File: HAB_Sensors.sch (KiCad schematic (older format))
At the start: 20 parts, among them U10 LM4030, U7 MCP9808T, U8 BME280, U9 LSM9DS1

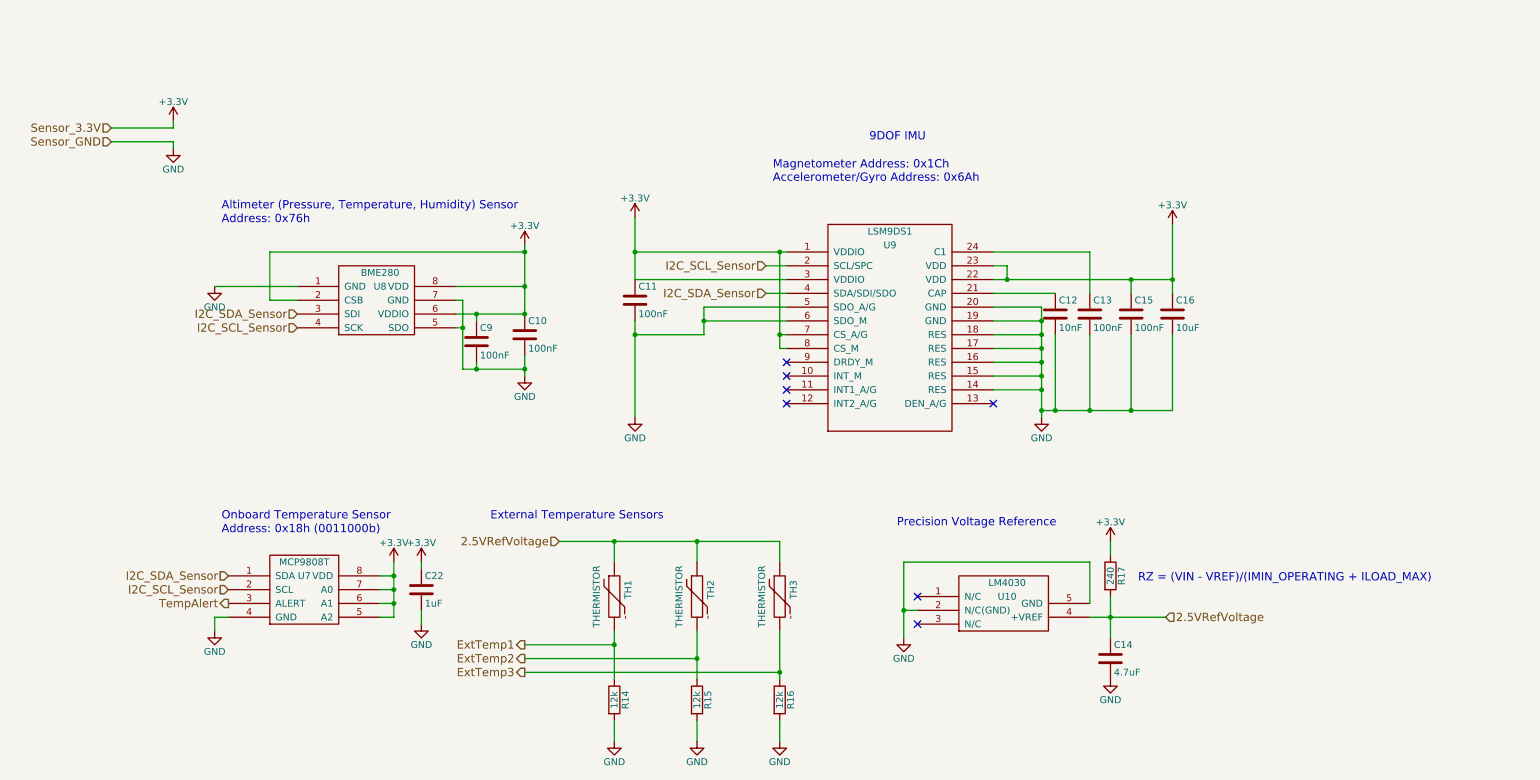
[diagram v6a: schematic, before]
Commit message: rev 2 of hab board in progress
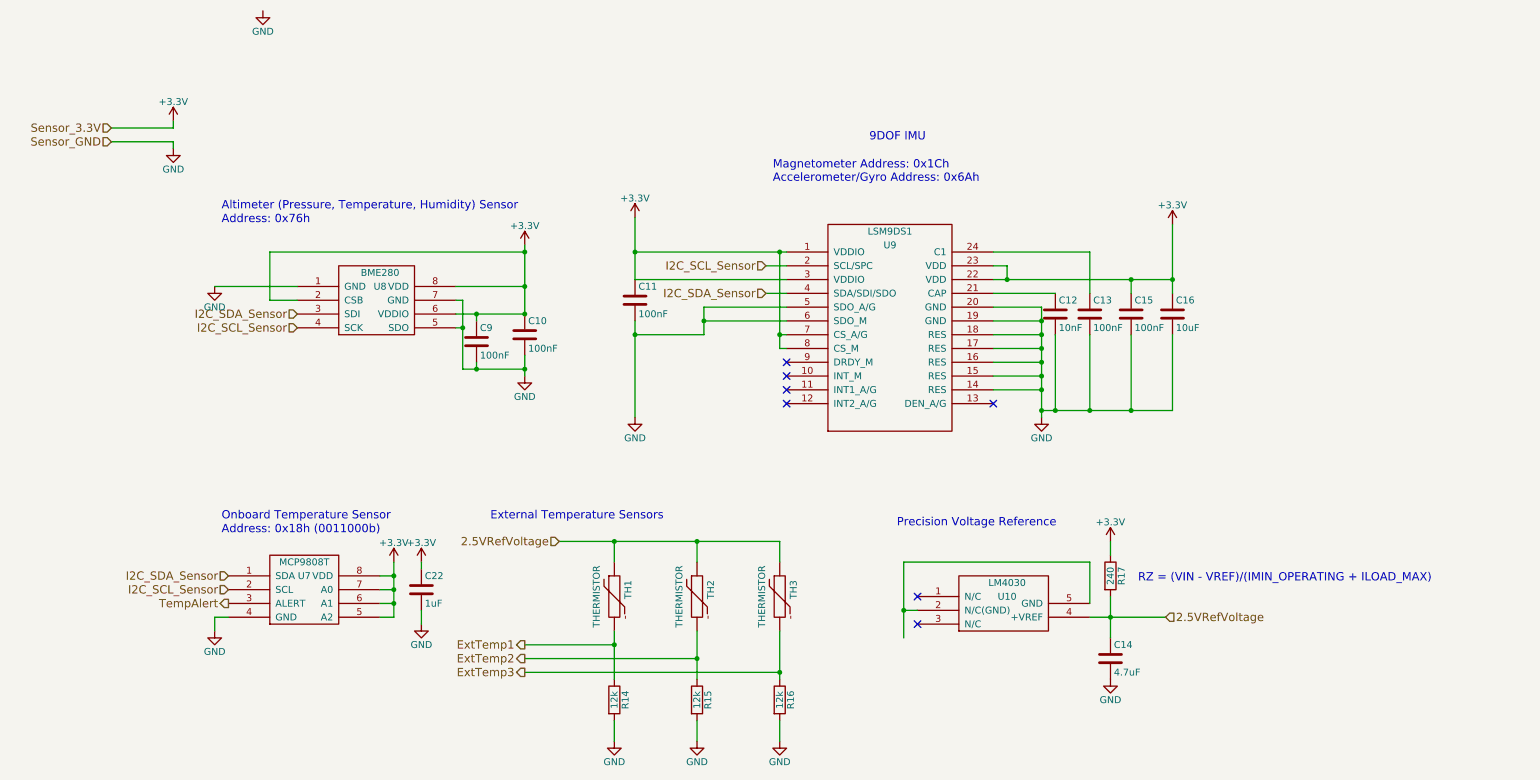
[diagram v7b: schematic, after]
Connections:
- net GND: no longer U10.2 (N/C(GND)), U10.5 (GND)
- new net: U10.2 (N/C(GND)), U10.5 (GND)
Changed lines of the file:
@@
 $EndComp
 $Comp
-L +3.3V #PWR039
+L +3.3V #PWR040
 U 1 1 56DF3EDE
 P 4250 1900
-F 0 "#PWR039" H 4250 1750 50  0001 C CNN
+F 0 "#PWR040" H 4250 1750 50  0001 C CNN
 F 1 "+3.3V" H 4250 2040 50  0000 C CNN
 F 2 "" H 4250 1900 50  0000 C CNN
@@
 $EndComp
 $Comp
-L +3.3V #PWR040
+L +3.3V #PWR041
 U 1 1 56DF3EFC
 P 3300 4200
-F 0 "#PWR040" H 3300 4050 50  0001 C CNN
+F 0 "#PWR041" H 3300 4050 50  0001 C CNN
 F 1 "+3.3V" H 3300 4340 50  0000 C CNN
 F 2 "" H 3300 4200 50  0000 C CNN
@@
 $EndComp
 $Comp
-L +3.3V #PWR041
+L +3.3V #PWR042
 U 1 1 56DF3F1A
 P 8950 1750
-F 0 "#PWR041" H 8950 1600 50  0001 C CNN
+F 0 "#PWR042" H 8950 1600 50  0001 C CNN
 F 1 "+3.3V" H 8950 1890 50  0000 C CNN
 F 2 "" H 8950 1750 50  0000 C CNN
@@
 $EndComp
 $Comp
-L +3.3V #PWR042
+L +3.3V #PWR043
 U 1 1 56DF3F56
 P 5050 1700
-F 0 "#PWR042" H 5050 1550 50  0001 C CNN
+F 0 "#PWR043" H 5050 1550 50  0001 C CNN
 F 1 "+3.3V" H 5050 1840 50  0000 C CNN
 F 2 "" H 5050 1700 50  0000 C CNN
@@
 $EndComp
 $Comp
-L GND #PWR043
+L GND #PWR044
 U 1 1 56DF3F74
 P 4250 2850
-F 0 "#PWR043" H 4250 2600 50  0001 C CNN
+F 0 "#PWR044" H 4250 2600 50  0001 C CNN
 F 1 "GND" H 4250 2700 50  0000 C CNN
 F 2 "" H 4250 2850 50  0000 C CNN
@@
 $EndComp
 $Comp
-L GND #PWR044
+L GND #PWR045
 U 1 1 56DF3F92
 P 2000 2200
-F 0 "#PWR044" H 2000 1950 50  0001 C CNN
+F 0 "#PWR045" H 2000 1950 50  0001 C CNN
 F 1 "GND" H 2000 2050 50  0000 C CNN
 F 2 "" H 2000 2200 50  0000 C CNN
@@
 $EndComp
 $Comp
-L GND #PWR045
+L GND #PWR046
 U 1 1 56DF3FCE
 P 2000 4700
-F 0 "#PWR045" H 2000 4450 50  0001 C CNN
+F 0 "#PWR046" H 2000 4450 50  0001 C CNN
 F 1 "GND" H 2000 4550 50  0000 C CNN
 F 2 "" H 2000 4700 50  0000 C CNN
@@
 $EndComp
 $Comp
-L GND #PWR046
+L GND #PWR047
 U 1 1 56DF3FEC
 P 8000 3150
-F 0 "#PWR046" H 8000 2900 50  0001 C CNN
+F 0 "#PWR047" H 8000 2900 50  0001 C CNN
 F 1 "GND" H 8000 3000 50  0000 C CNN
 F 2 "" H 8000 3150 50  0000 C CNN
@@
 I2C_SCL_Sensor
 $Comp
-L GND #PWR047
+L GND #PWR048
 U 1 1 56DF8E0E
 P 5050 3150
-F 0 "#PWR047" H 5050 2900 50  0001 C CNN
+F 0 "#PWR048" H 5050 2900 50  0001 C CNN
 F 1 "GND" H 5050 3000 50  0000 C CNN
 F 2 "" H 5050 3150 50  0000 C CNN
@@
 $EndComp
 $Comp
-L GND #PWR048
+L GND #PWR049
 U 1 1 56E7BBB4
-P 7000 4750
-F 0 "#PWR048" H 7000 4500 50  0001 C CNN
-F 1 "GND" H 7000 4600 50  0000 C CNN
-F 2 "" H 7000 4750 50  0000 C CNN
-F 3 "" H 7000 4750 50  0000 C CNN
-	1    7000 4750
+P 2350 200
+F 0 "#PWR049" H 2350 -50 50  0001 C CNN
+F 1 "GND" H 2350 50  50  0000 C CNN
+F 2 "" H 2350 200 50  0000 C CNN
+F 3 "" H 2350 200 50  0000 C CNN
+	1    2350 200
 	1    0    0    -1
 $EndComp
@@
 2.5VRefVoltage
 $Comp
-L +3.3V #PWR049
+L +3.3V #PWR050
 U 1 1 56E7C137
 P 8500 4050
-F 0 "#PWR049" H 8500 3900 50  0001 C CNN
+F 0 "#PWR050" H 8500 3900 50  0001 C CNN
 F 1 "+3.3V" H 8500 4190 50  0000 C CNN
 F 2 "" H 8500 4050 50  0000 C CNN
@@
 $EndComp
 $Comp
-L GND #PWR050
+L GND #PWR051
 U 1 1 56E7C40E
 P 8500 5050
-F 0 "#PWR050" H 8500 4800 50  0001 C CNN
+F 0 "#PWR051" H 8500 4800 50  0001 C CNN
 F 1 "GND" H 8500 4900 50  0000 C CNN
 F 2 "" H 8500 5050 50  0000 C CNN
@@
 $EndComp
 $Comp
-L GND #PWR051
+L GND #PWR052
 U 1 1 56E7CBC6
 P 4900 5500
-F 0 "#PWR051" H 4900 5250 50  0001 C CNN
+F 0 "#PWR052" H 4900 5250 50  0001 C CNN
 F 1 "GND" H 4900 5350 50  0000 C CNN
 F 2 "" H 4900 5500 50  0000 C CNN
@@
 $EndComp
 $Comp
-L GND #PWR052
+L GND #PWR053
 U 1 1 56E7CBF2
 P 6100 5500
-F 0 "#PWR052" H 6100 5250 50  0001 C CNN
+F 0 "#PWR053" H 6100 5250 50  0001 C CNN
 F 1 "GND" H 6100 5350 50  0000 C CNN
 F 2 "" H 6100 5500 50  0000 C CNN
@@
 Sensor_3.3V
 $Comp
-L +3.3V #PWR053
+L +3.3V #PWR054
 U 1 1 56E8E1D1
 P 1700 1000
-F 0 "#PWR053" H 1700 850 50  0001 C CNN
+F 0 "#PWR054" H 1700 850 50  0001 C CNN
 F 1 "+3.3V" H 1700 1140 50  0000 C CNN
 F 2 "" H 1700 1000 50  0000 C CNN
@@
 Sensor_GND
 $Comp
-L GND #PWR054
+L GND #PWR055
 U 1 1 56E8E7BD
 P 1700 1200
-F 0 "#PWR054" H 1700 950 50  0001 C CNN
+F 0 "#PWR055" H 1700 950 50  0001 C CNN
 F 1 "GND" H 1700 1050 50  0000 C CNN
 F 2 "" H 1700 1200 50  0000 C CNN
@@
 $EndComp
 $Comp
-L GND #PWR055
+L GND #PWR056
 U 1 1 56F543F0
 P 5500 5500
-F 0 "#PWR055" H 5500 5250 50  0001 C CNN
+F 0 "#PWR056" H 5500 5250 50  0001 C CNN
 F 1 "GND" H 5500 5350 50  0000 C CNN
 F 2 "" H 5500 5500 50  0000 C CNN
@@
 $EndComp
 $Comp
-L +3.3V #PWR056
+L +3.3V #PWR057
 U 1 1 57026FD6
 P 3500 4200
-F 0 "#PWR056" H 3500 4050 50  0001 C CNN
+F 0 "#PWR057" H 3500 4050 50  0001 C CNN
 F 1 "+3.3V" H 3500 4340 50  0000 C CNN
 F 2 "" H 3500 4200 50  0000 C CNN
@@
 	3500 4200 3500 4250
 $Comp
-L GND #PWR057
+L GND #PWR058
 U 1 1 570270BB
 P 3500 4650
-F 0 "#PWR057" H 3500 4400 50  0001 C CNN
+F 0 "#PWR058" H 3500 4400 50  0001 C CNN
 F 1 "GND" H 3500 4500 50  0000 C CNN
 F 2 "" H 3500 4650 50  0000 C CNN
